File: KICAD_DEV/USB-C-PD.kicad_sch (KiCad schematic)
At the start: 36 parts, among them J1 USB_C_Receptacle_USB2.0_14P, Q1 NMOS, U2 TPS26750, U3 TPD4S480

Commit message: updating some stuff
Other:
- moved on the sheet: R10, R11, R12, R7, R8, R9

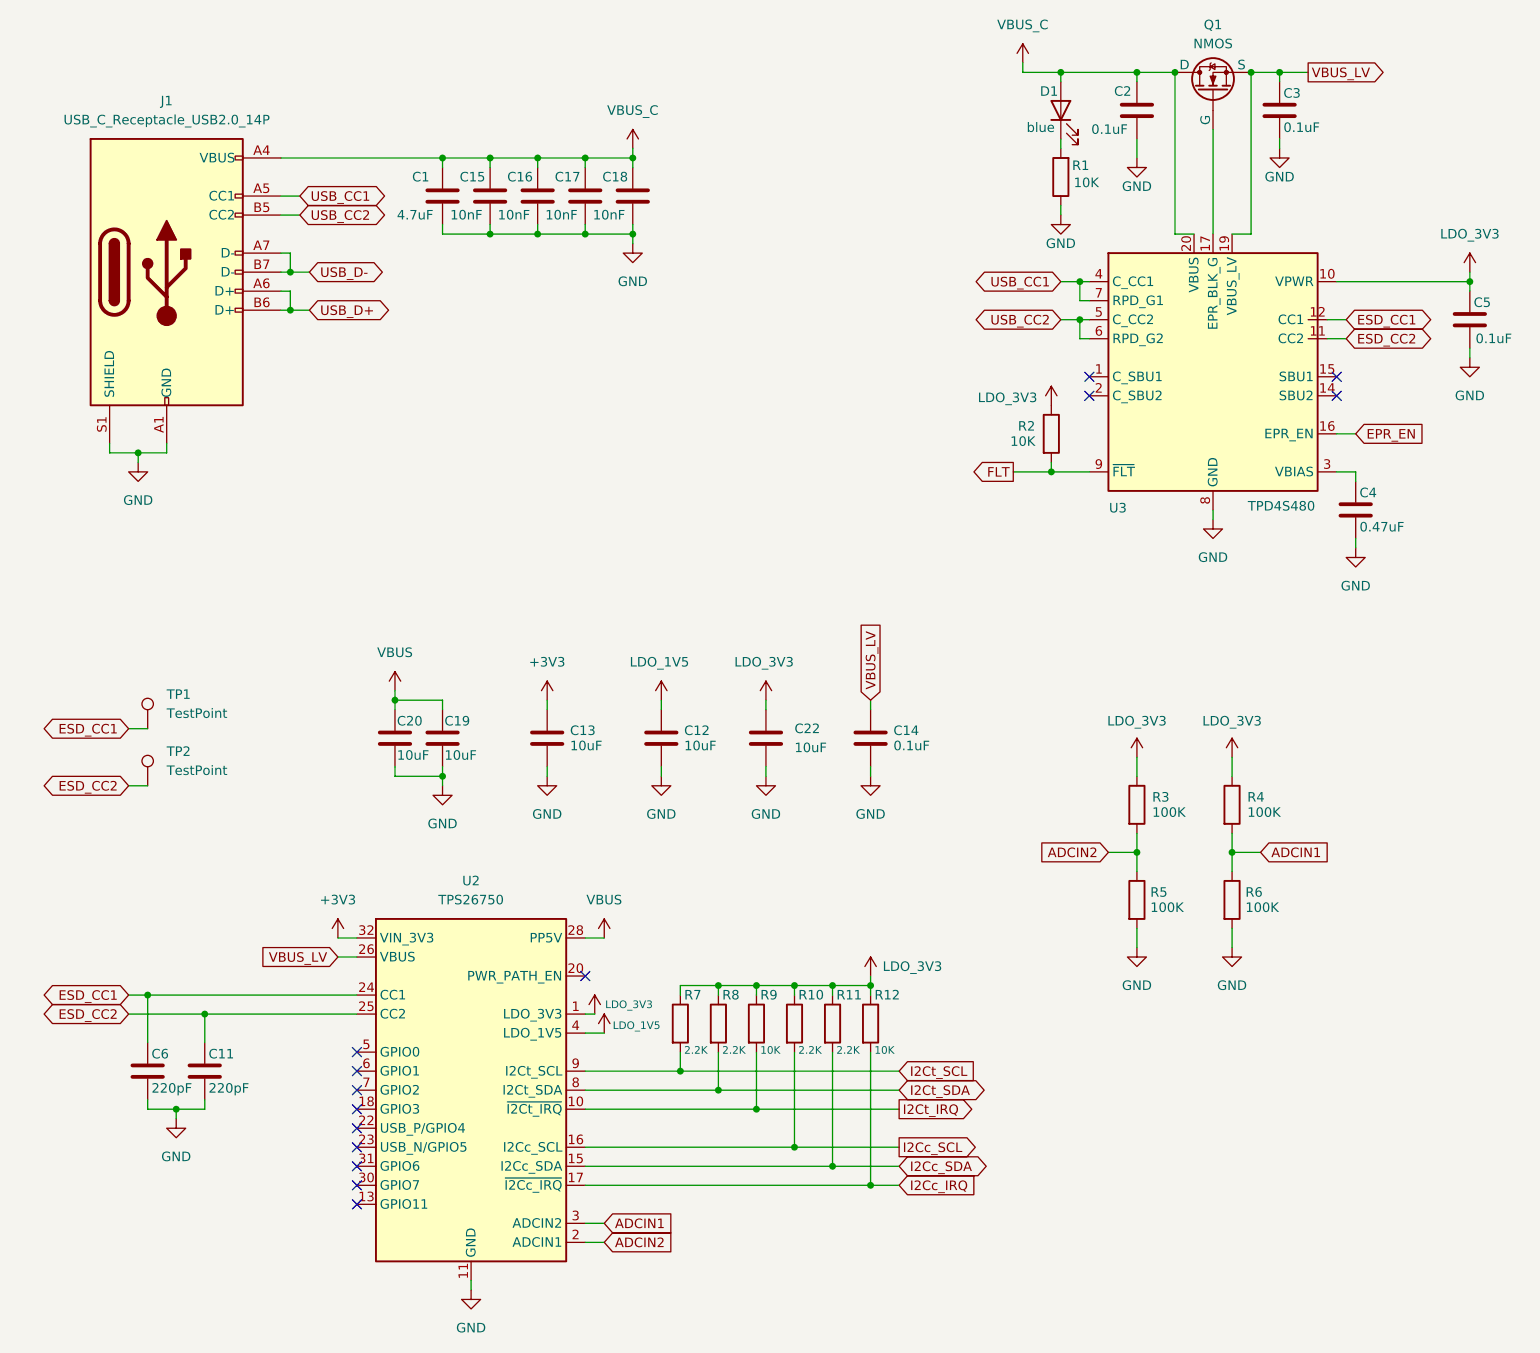
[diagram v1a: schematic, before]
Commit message: switching to a PSU
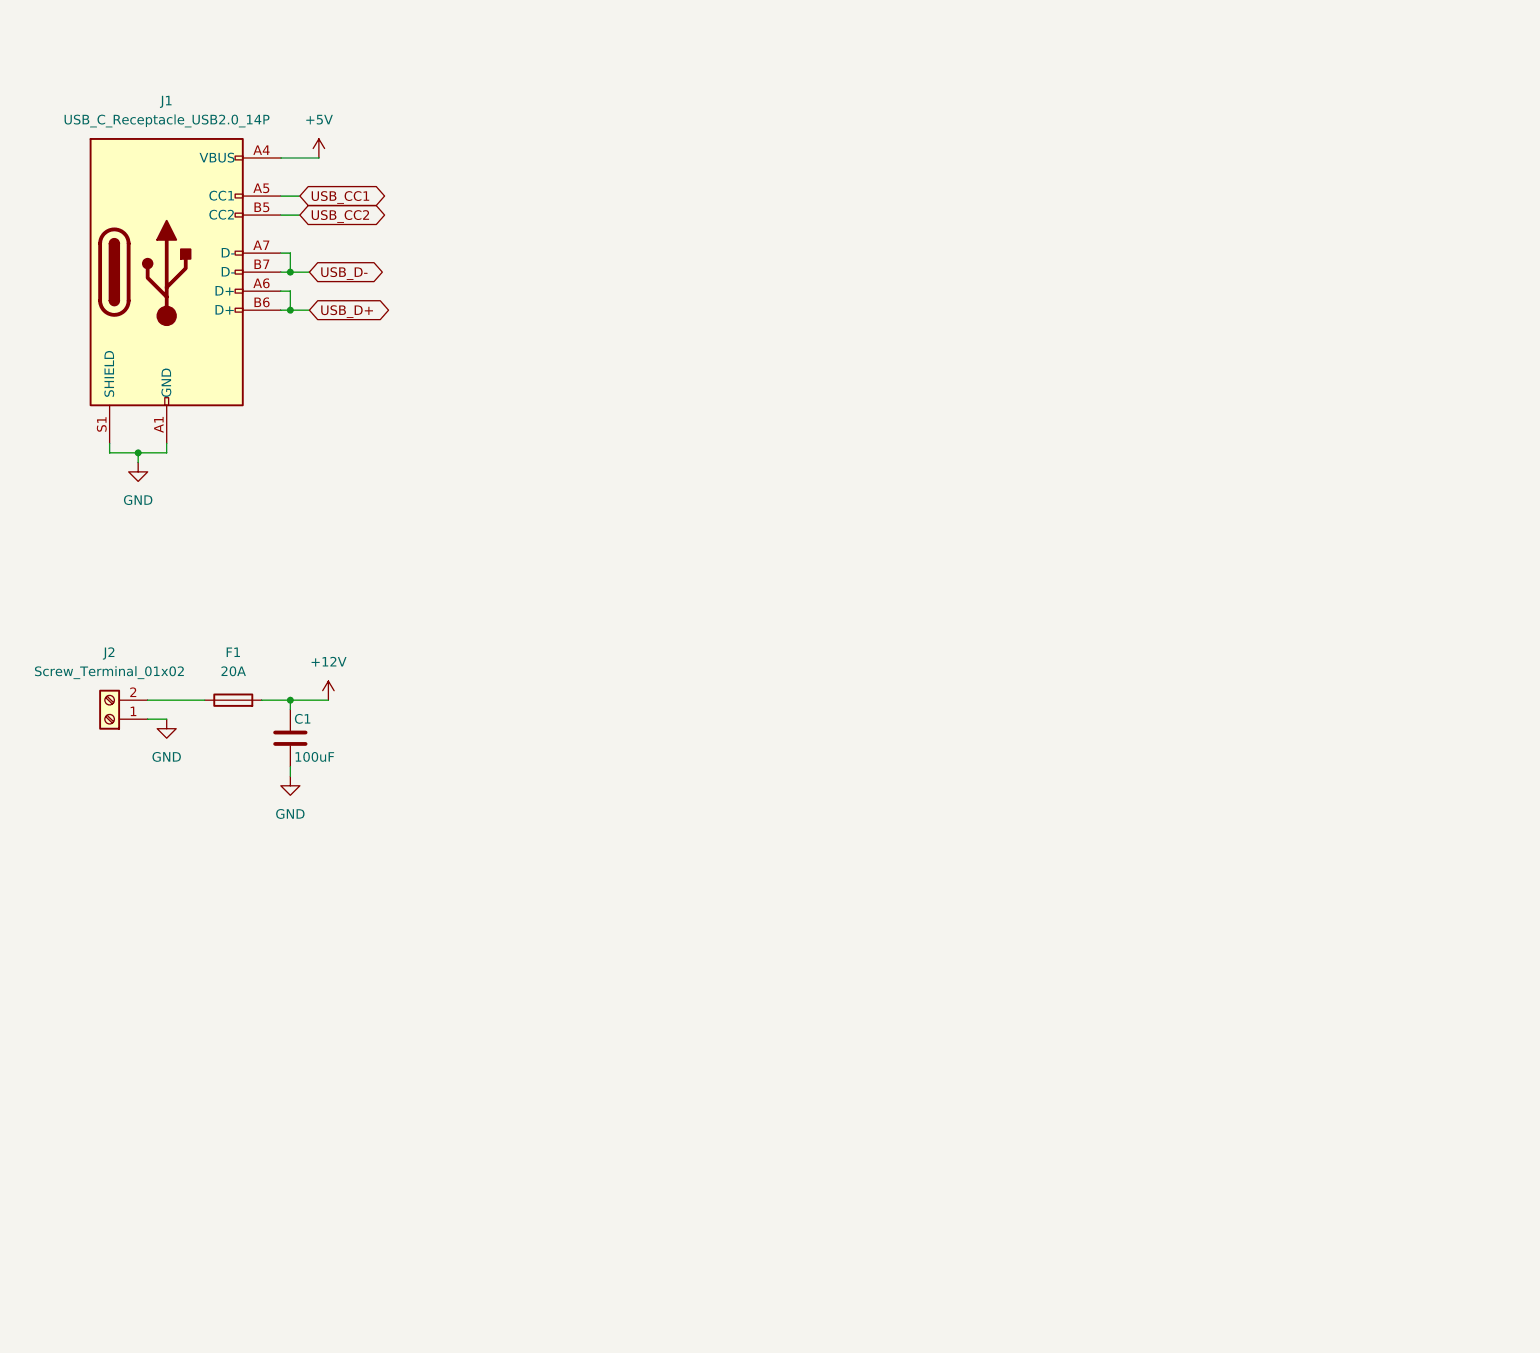
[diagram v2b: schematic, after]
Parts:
- removed C11, C6: 220pF, symbol Device:C
- removed C12, C13, C19, C20, C22: 10uF, symbol Device:C
- removed C14, C2, C3, C5: 0.1uF, symbol Device:C
- removed C15, C16, C17, C18: 10nF, symbol Device:C
- removed C4: 0.47uF, symbol Device:C
- removed D1: blue, symbol Device:LED
- removed Q1: NMOS, symbol Simulation_SPICE:NMOS
- removed R1, R12, R2, R9: 10K, symbol Device:R
- removed R10, R11, R7, R8: 2.2K, symbol Device:R
- removed R3, R4, R5, R6: 100K, symbol Device:R
- removed TP1, TP2: TestPoint, symbol Connector:TestPoint
- removed U2: TPS26750, Package_DFN_QFN:VQFN-32-1EP_4x4mm_P0.4mm_EP2.8x2.8mm_ThermalVias, symbol kai-library:TPS26750
- removed U3: TPD4S480, Package_DFN_QFN:WQFN-20-1EP_3x3mm_P0.4mm_EP1.7x1.7mm_ThermalVias, symbol kai-library:TPD4S480
- added F1: 20A, symbol Device:Fuse
- added J2: Screw_Terminal_01x02, symbol Connector:Screw_Terminal_01x02
- C1: value 4.7uF -> 100uF
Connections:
- net GND: now also J2.1 (Pin_1)
- net VBUS_C renamed +5V
- net +5V: no longer C1.1
- new net: F1.1, J2.2 (Pin_2)
- new net +12V: C1.1, F1.2
- no-connect marks 14 -> 0

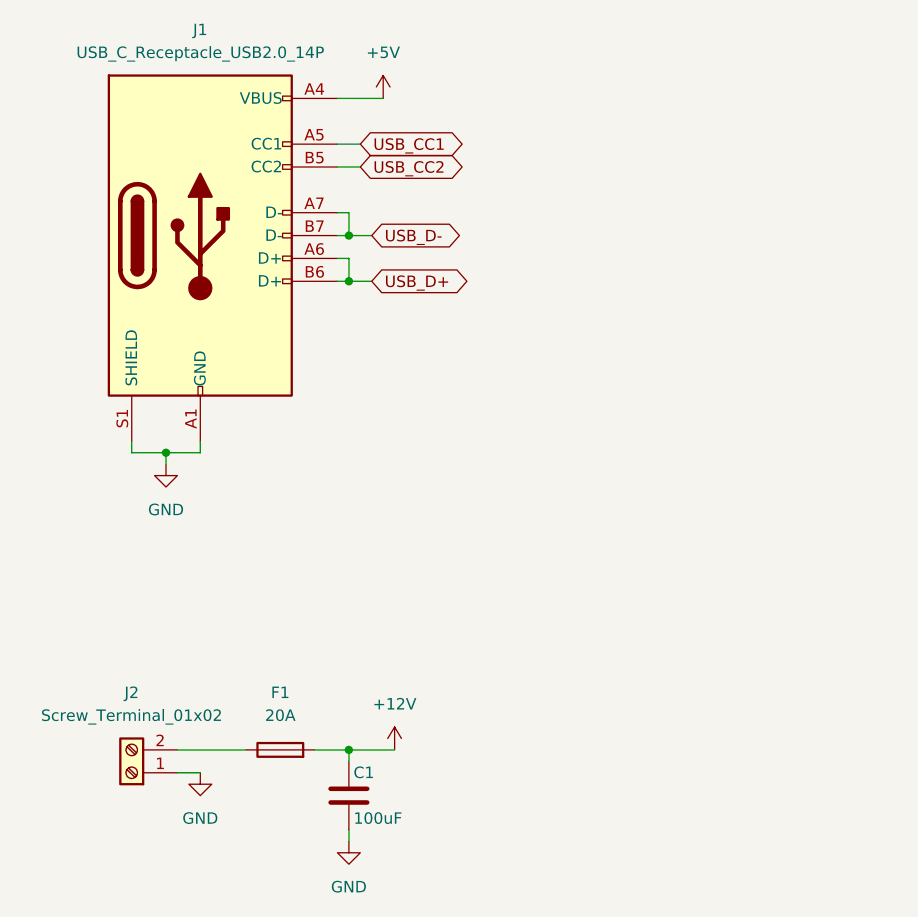
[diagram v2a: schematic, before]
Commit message: ESD Protection!
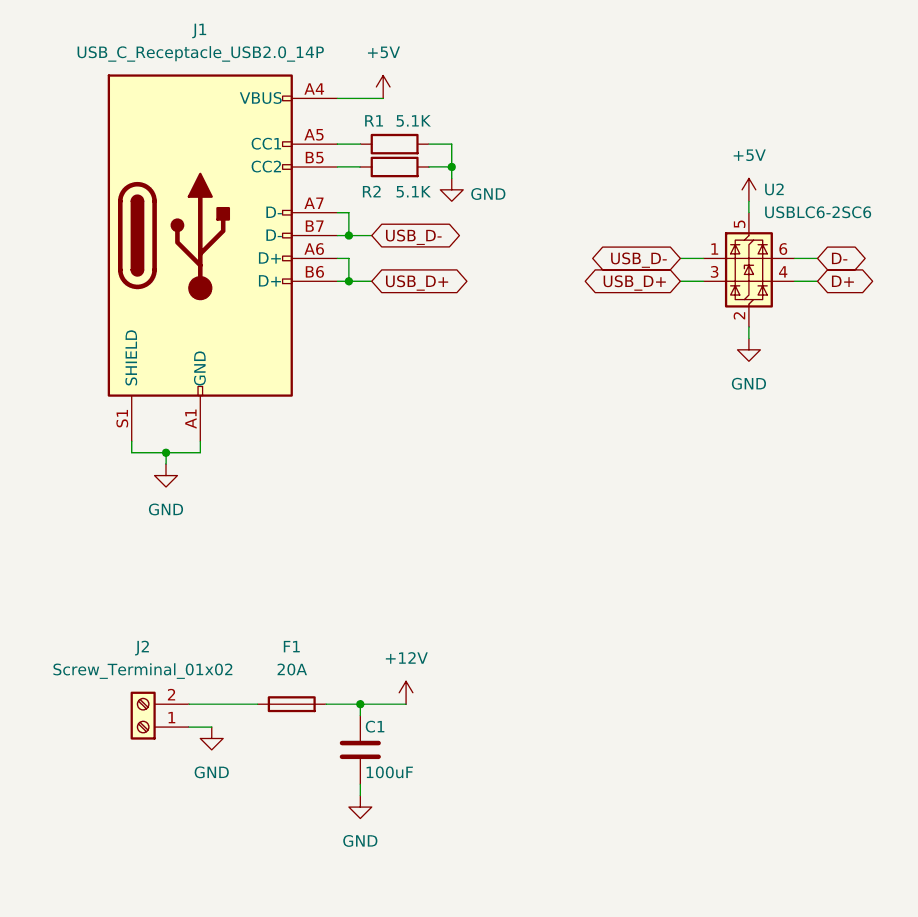
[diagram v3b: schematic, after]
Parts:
- added R1, R2: 5.1K, symbol Device:R
- added U2: USBLC6-2SC6, Package_TO_SOT_SMD:SOT-23-6, symbol Power_Protection:USBLC6-2SC6
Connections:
- net +5V: now also U2.5 (VBUS)
- net GND: now also R1.2, R2.2, U2.2 (GND)
- net USB_D+: now also U2.3 (I/O2)
- net USB_D-: now also U2.1 (I/O1)
- net USB_CC1: no longer names the net of J1.A5 (CC1)
- net USB_CC1: now also R1.1
- net USB_CC2: no longer names the net of J1.B5 (CC2)
- net USB_CC2: now also R2.1
- new net D+: U2.4 (I/O2)
- new net D-: U2.6 (I/O1)
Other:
- moved on the sheet: C1, F1, J2
